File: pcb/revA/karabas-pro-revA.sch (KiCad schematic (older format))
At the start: 130 parts, among them CON1 CF-CARD, CON2 SD, CON3 VGA, CON4 Joystick, CON5 Keyboard, CON6 Mouse, CON7 Audio, CON8 5V DC, J1 Floppy, J2 FPGA JTAG, J3 Floppy 5V, J4 uBus, J5 AVR JTAG, J6 AVR UART, SW1 SW_Push, SW2 SW_Push, U1 EP4CE6E22C8N, U10 ESP-12E, U11 TDA1543, U12 AMS1117-3.3, U13 AMS1117-2.5, U14 AMS1117-1.2, U17 74LS06, U18 74LS38, U2 CY62167EV30, U3 W25Q32JVSS, U4 EPM3128ATC100-5, U5 ATMEGA328-AU, U6 MB8877A, U7 TXB0104PW, U8 TXB0104PW, U9 DS1307Z+, X1 SG-7050CAN, Y1 32768Hz, Y2 16MHz

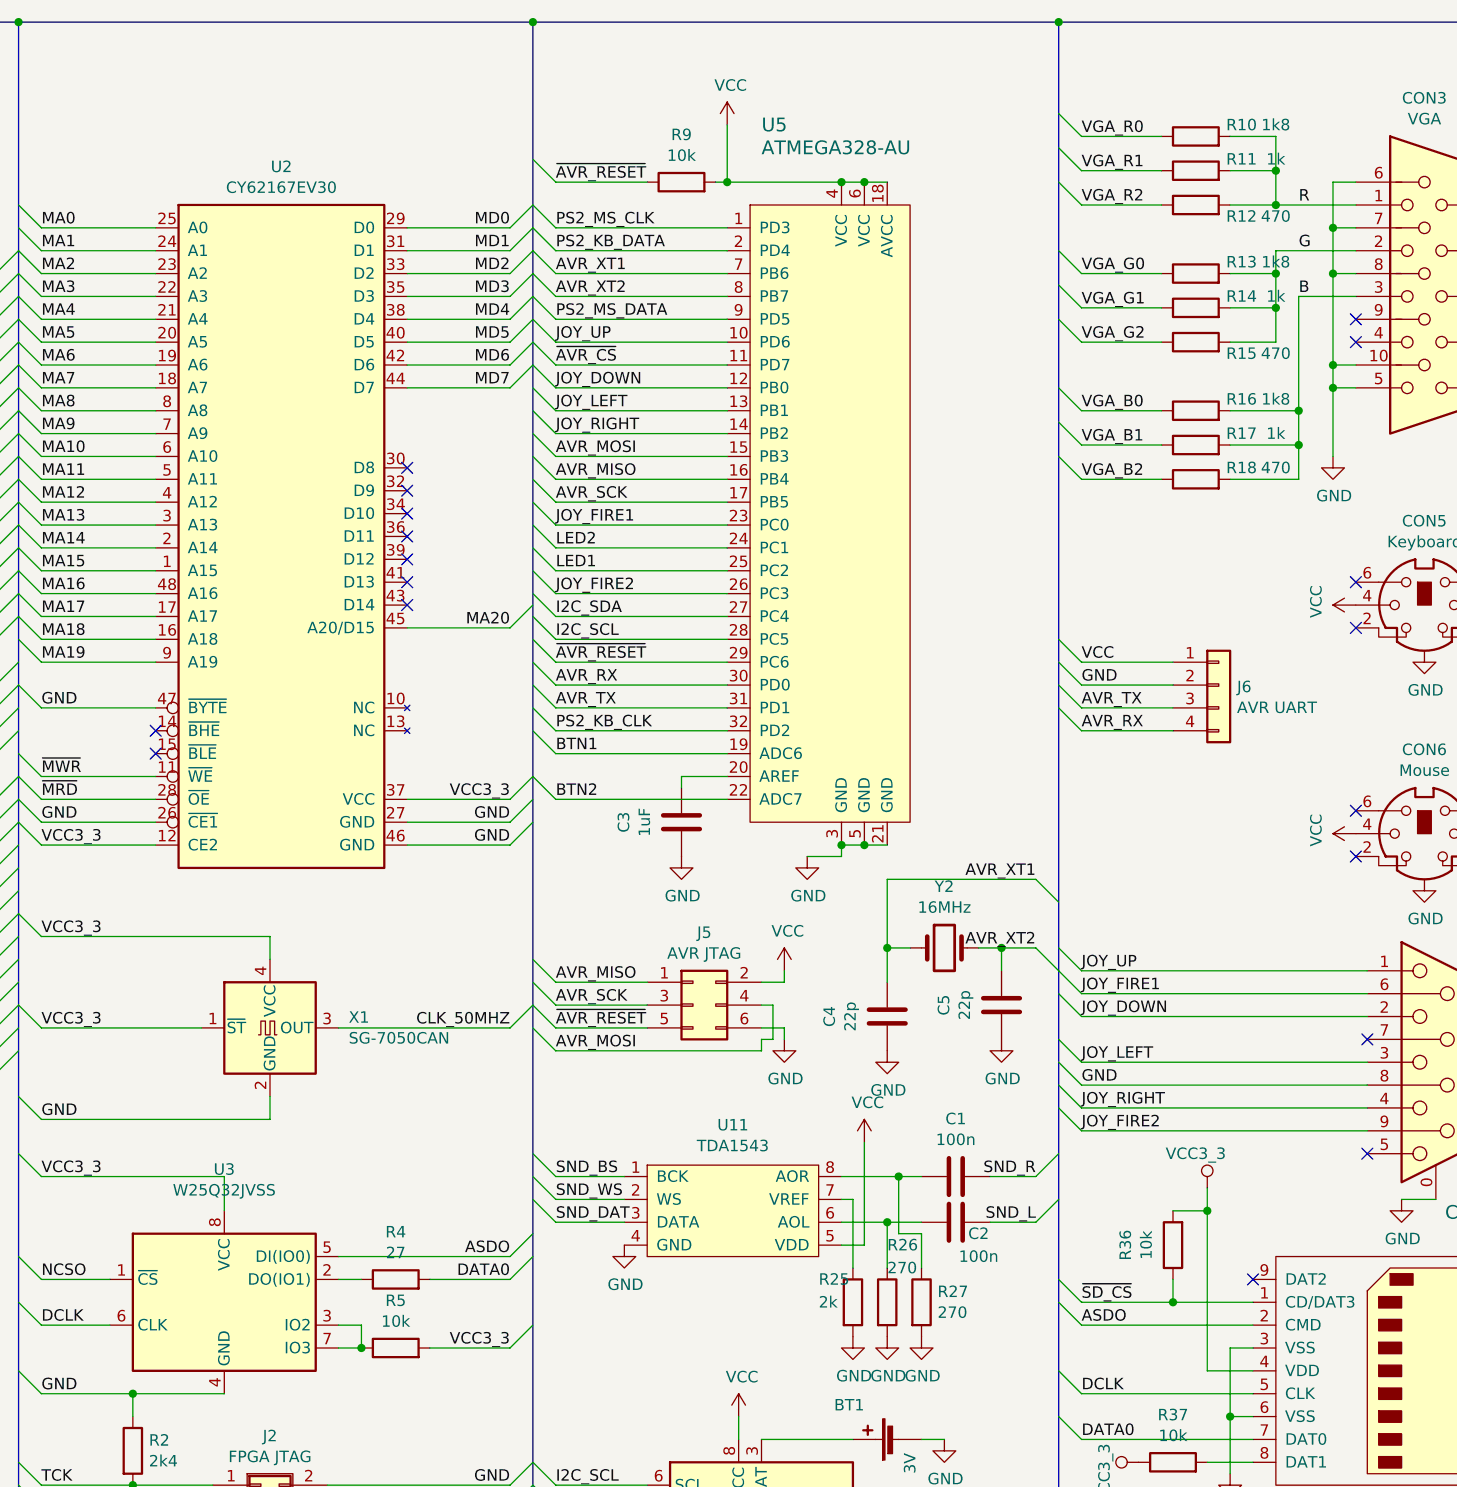
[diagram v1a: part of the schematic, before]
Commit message: Added rev.A documentation
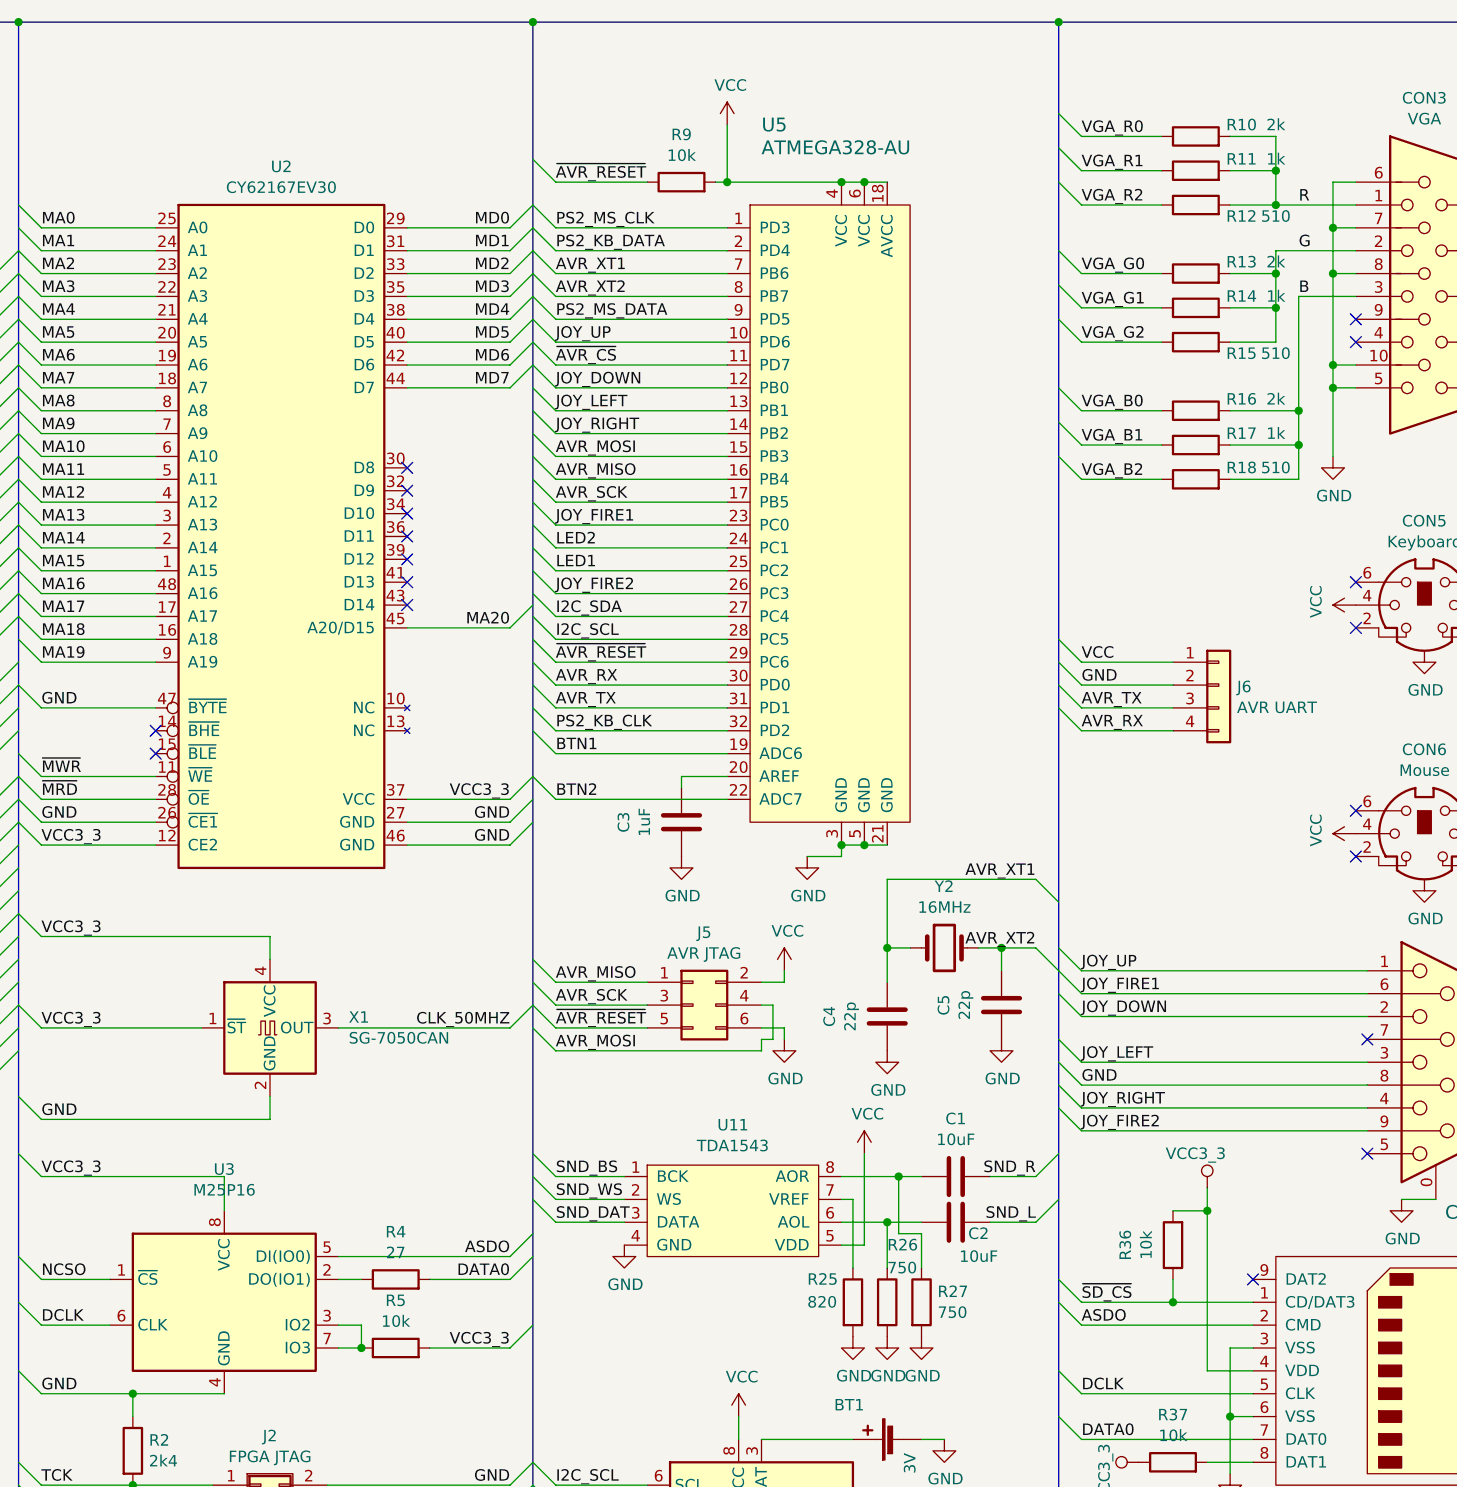
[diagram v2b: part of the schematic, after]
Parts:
- C1, C2: value 100n -> 10uF
- R10, R13, R16: value 1k8 -> 2k
- R12, R15, R18: value 470 -> 510
- R25: value 2k -> 820
- R26, R27: value 270 -> 750
- U3: value W25Q32JVSS -> M25P16
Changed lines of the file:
@@
 encoding utf-8
 Sheet 1 1
-Title "Karabas FPGA"
-Date ""
+Title "Karabas Pro"
+Date "2020-07-25"
 Rev "A"
 Comp ""
@@
 P 7400 6300
 F 0 "U3" H 7400 6881 50  0000 C CNN
-F 1 "W25Q32JVSS" H 7400 6790 50  0000 C CNN
+F 1 "M25P16" H 7400 6790 50  0000 C CNN
 F 2 "Package_SO:SOIC-8_5.23x5.23mm_P1.27mm" H 7400 6300 50  0001 C CNN
 F 3 "http://www.winbond.com/resource-files/w25q32jv%20revg%2003272018%20plus.pdf" H 7400 6300 50  0001 C CNN
@@
 P 11650 1200
 F 0 "R10" V 11700 1000 50  0000 C CNN
-F 1 "1k8" V 11700 850 50  0000 C CNN
+F 1 "2k" V 11700 850 50  0000 C CNN
 F 2 "Resistor_SMD:R_0805_2012Metric_Pad1.15x1.40mm_HandSolder" V 11580 1200 50  0001 C CNN
 F 3 "~" H 11650 1200 50  0001 C CNN
@@
 P 11650 1500
 F 0 "R12" V 11600 1300 50  0000 C CNN
-F 1 "470" V 11600 1150 50  0000 C CNN
+F 1 "510" V 11600 1150 50  0000 C CNN
 F 2 "Resistor_SMD:R_0805_2012Metric_Pad1.15x1.40mm_HandSolder" V 11580 1500 50  0001 C CNN
 F 3 "~" H 11650 1500 50  0001 C CNN
@@
 P 11650 1800
 F 0 "R13" V 11700 1600 50  0000 C CNN
-F 1 "1k8" V 11700 1450 50  0000 C CNN
+F 1 "2k" V 11700 1450 50  0000 C CNN
 F 2 "Resistor_SMD:R_0805_2012Metric_Pad1.15x1.40mm_HandSolder" V 11580 1800 50  0001 C CNN
 F 3 "~" H 11650 1800 50  0001 C CNN
@@
 P 11650 2100
 F 0 "R15" V 11600 1900 50  0000 C CNN
-F 1 "470" V 11600 1750 50  0000 C CNN
+F 1 "510" V 11600 1750 50  0000 C CNN
 F 2 "Resistor_SMD:R_0805_2012Metric_Pad1.15x1.40mm_HandSolder" V 11580 2100 50  0001 C CNN
 F 3 "~" H 11650 2100 50  0001 C CNN
@@
 P 11650 2400
 F 0 "R16" V 11700 2200 50  0000 C CNN
-F 1 "1k8" V 11700 2050 50  0000 C CNN
+F 1 "2k" V 11700 2050 50  0000 C CNN
 F 2 "Resistor_SMD:R_0805_2012Metric_Pad1.15x1.40mm_HandSolder" V 11580 2400 50  0001 C CNN
 F 3 "~" H 11650 2400 50  0001 C CNN
@@
 P 11650 2700
 F 0 "R18" V 11700 2500 50  0000 C CNN
-F 1 "470" V 11700 2350 50  0000 C CNN
+F 1 "510" V 11700 2350 50  0000 C CNN
 F 2 "Resistor_SMD:R_0805_2012Metric_Pad1.15x1.40mm_HandSolder" V 11580 2700 50  0001 C CNN
 F 3 "~" H 11650 2700 50  0001 C CNN
@@
 U 1 1 5F614B1C
 P 10150 6300
-F 0 "R25" H 10000 6400 50  0000 L CNN
-F 1 "2k" H 10000 6300 50  0000 L CNN
+F 0 "R25" H 9950 6400 50  0000 L CNN
+F 1 "820" H 9950 6300 50  0000 L CNN
 F 2 "Resistor_SMD:R_0805_2012Metric_Pad1.15x1.40mm_HandSolder" V 10080 6300 50  0001 C CNN
 F 3 "~" H 10150 6300 50  0001 C CNN
@@
 L power:VCC #PWR0124
 U 1 1 5F66A4E2
-P 10200 5600
-F 0 "#PWR0124" H 10200 5450 50  0001 C CNN
-F 1 "VCC" H 10215 5773 50  0000 C CNN
-F 2 "" H 10200 5600 50  0001 C CNN
-F 3 "" H 10200 5600 50  0001 C CNN
-	1    10200 5600
+P 10200 5650
+F 0 "#PWR0124" H 10200 5500 50  0001 C CNN
+F 1 "VCC" H 10215 5823 50  0000 C CNN
+F 2 "" H 10200 5650 50  0001 C CNN
+F 3 "" H 10200 5650 50  0001 C CNN
+	1    10200 5650
 	1    0    0    -1
 $EndComp
@@
 P 10300 6300
 F 0 "R26" H 10300 6550 50  0000 L CNN
-F 1 "270" H 10300 6450 50  0000 L CNN
+F 1 "750" H 10300 6450 50  0000 L CNN
 F 2 "Resistor_SMD:R_0805_2012Metric_Pad1.15x1.40mm_HandSolder" V 10230 6300 50  0001 C CNN
 F 3 "~" H 10300 6300 50  0001 C CNN
@@
 P 10450 6300
 F 0 "R27" H 10520 6346 50  0000 L CNN
-F 1 "270" H 10520 6255 50  0000 L CNN
+F 1 "750" H 10520 6255 50  0000 L CNN
 F 2 "Resistor_SMD:R_0805_2012Metric_Pad1.15x1.40mm_HandSolder" V 10380 6300 50  0001 C CNN
 F 3 "~" H 10450 6300 50  0001 C CNN
@@
 	10100 6050 10200 6050
 Wire Wire Line
-	10200 6050 10200 5600
+	10200 6050 10200 5650
 Wire Wire Line
 	10100 5950 10300 5950
@@
 P 10600 5750
 F 0 "C1" V 10852 5750 50  0000 C CNN
-F 1 "100n" V 10761 5750 50  0000 C CNN
+F 1 "10uF" V 10761 5750 50  0000 C CNN
 F 2 "Capacitor_SMD:C_0805_2012Metric_Pad1.15x1.40mm_HandSolder" H 10638 5600 50  0001 C CNN
 F 3 "~" H 10600 5750 50  0001 C CNN
@@
 P 10600 5950
 F 0 "C2" V 10550 5850 50  0000 C CNN
-F 1 "100n" V 10450 5850 50  0000 C CNN
+F 1 "10uF" V 10450 5850 50  0000 C CNN
 F 2 "Capacitor_SMD:C_0805_2012Metric_Pad1.15x1.40mm_HandSolder" H 10638 5800 50  0001 C CNN
 F 3 "~" H 10600 5950 50  0001 C CNN
@@
 Wire Wire Line
 	18750 11050 18300 11050
+Connection ~ 18300 11050
 Wire Bus Line
 	14200 10200 14200 11000
@@
 Wire Bus Line
 	8750 700  8750 11450
-Connection ~ 18300 11050
 $EndSCHEMATC
